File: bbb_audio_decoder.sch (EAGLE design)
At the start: 185 parts, among them IC1 OPA2134, IC2 LM317, IC3 LM337, IC4 OPA2134, IC5 OPA2134, IC6 OPA2134, IC7 LM317, P1 PLR135/T9, Q2 BS170, U1 PCM1690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

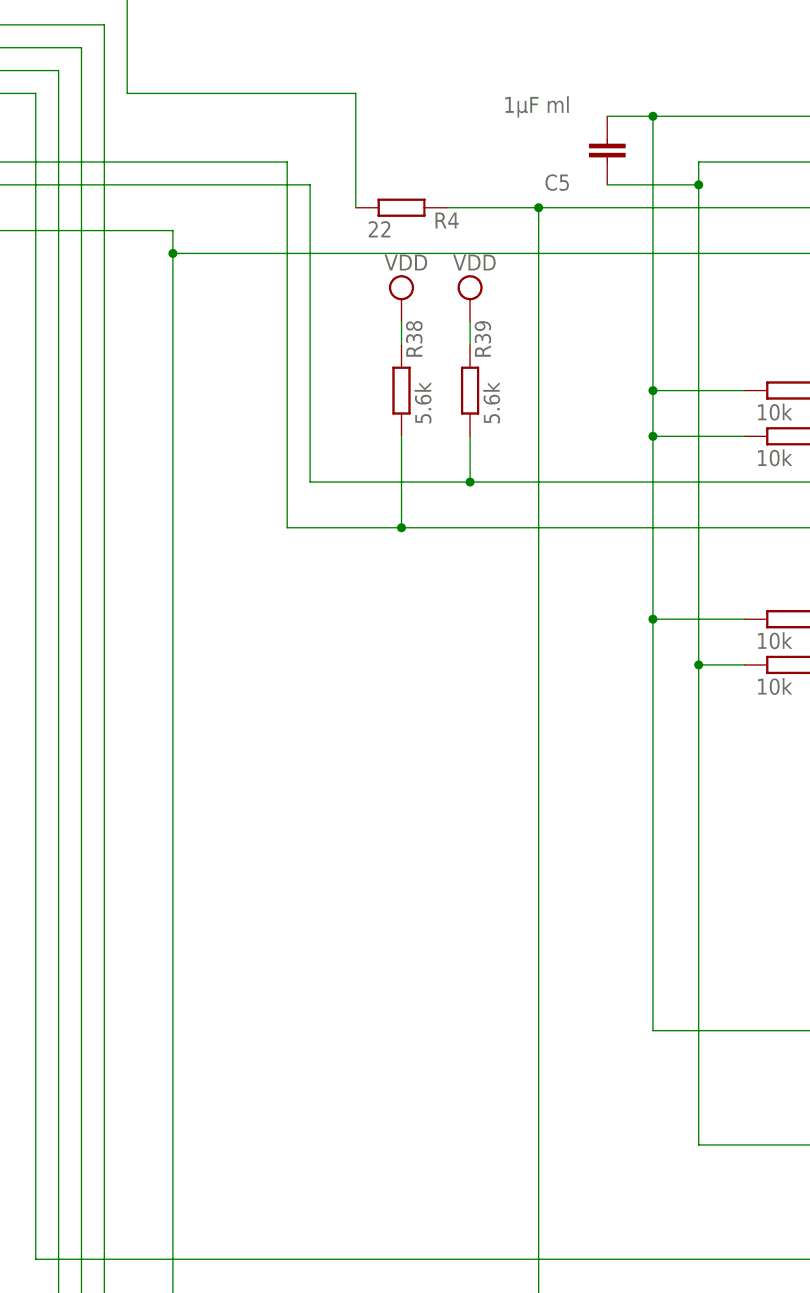
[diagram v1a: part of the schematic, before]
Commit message: Added molex 22-27-2041 connector for LCD
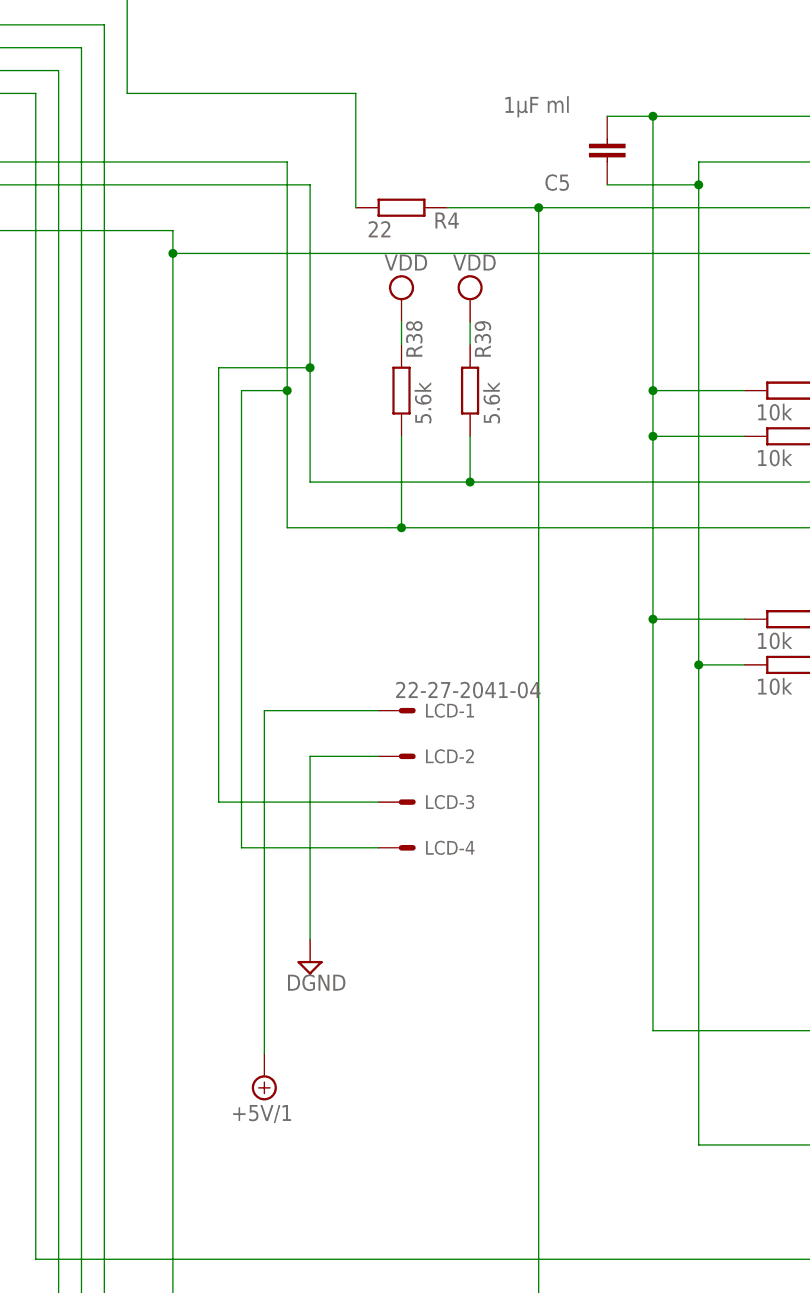
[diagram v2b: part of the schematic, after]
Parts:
- added LCD: 22-27-2041-04, con-molex:22-27-2041-04
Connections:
- net DGND: now also LCD-2.S
- net SCL: now also LCD-4.S
- net SDA: now also LCD-3.S
- net VDD_5V: now also LCD-1.S
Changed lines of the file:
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@@
 <grid distance="0.1" unitdist="inch" unit="inch" style="lines" multiple="1" display="no" altdistance="0.01" altunitdist="inch" altunit="inch"/>
 <layers>
-<layer number="1" name="Top" color="4" fill="1" visible="yes" active="no"/>
-<layer number="2" name="Route2" color="1" fill="3" visible="yes" active="no"/>
-<layer number="3" name="Route3" color="4" fill="3" visible="yes" active="no"/>
-<layer number="14" name="Route14" color="1" fill="6" visible="yes" active="no"/>
-<layer number="15" name="Route15" color="4" fill="6" visible="yes" active="no"/>
-<layer number="16" name="Bottom" color="1" fill="1" visible="yes" active="no"/>
-<layer number="17" name="Pads" color="2" fill="1" visible="yes" active="no"/>
-<layer number="18" name="Vias" color="2" fill="1" visible="yes" active="no"/>
-<layer number="19" name="Unrouted" color="6" fill="1" visible="yes" active="no"/>
-<layer number="20" name="Dimension" color="15" fill="1" visible="yes" active="no"/>
-<layer number="21" name="tPlace" color="7" fill="1" visible="yes" active="no"/>
-<layer number="22" name="bPlace" color="7" fill="1" visible="yes" active="no"/>
-<layer number="23" name="tOrigins" color="15" fill="1" visible="yes" active="no"/>
-<layer number="24" name="bOrigins" color="15" fill="1" visible="yes" active="no"/>
-<layer number="25" name="tNames" color="7" fill="1" visible="yes" active="no"/>
-<layer number="26" name="bNames" color="7" fill="1" visible="yes" active="no"/>
-<layer number="27" name="tValues" color="7" fill="1" visible="yes" active="no"/>
-<layer number="28" name="bValues" color="7" fill="1" visible="yes" active="no"/>
+<layer number="1" name="Top" color="4" fill="1" visible="no" active="no"/>
+<layer number="2" name="Route2" color="1" fill="3" visible="no" active="no"/>
+<layer number="3" name="Route3" color="4" fill="3" visible="no" active="no"/>
+<layer number="14" name="Route14" color="1" fill="6" visible="no" active="no"/>
+<layer number="15" name="Route15" color="4" fill="6" visible="no" active="no"/>
+<layer number="16" name="Bottom" color="1" fill="1" visible="no" active="no"/>
+<layer number="17" name="Pads" color="2" fill="1" visible="no" active="no"/>
+<layer number="18" name="Vias" color="2" fill="1" visible="no" active="no"/>
+<layer number="19" name="Unrouted" color="6" fill="1" visible="no" active="no"/>
+<layer number="20" name="Dimension" color="15" fill="1" visible="no" active="no"/>
+<layer number="21" name="tPlace" color="7" fill="1" visible="no" active="no"/>
+<layer number="22" name="bPlace" color="7" fill="1" visible="no" active="no"/>
+<layer number="23" name="tOrigins" color="15" fill="1" visible="no" active="no"/>
+<layer number="24" name="bOrigins" color="15" fill="1" visible="no" active="no"/>
+<layer number="25" name="tNames" color="7" fill="1" visible="no" active="no"/>
+<layer number="26" name="bNames" color="7" fill="1" visible="no" active="no"/>
+<layer number="27" name="tValues" color="7" fill="1" visible="no" active="no"/>
+<layer number="28" name="bValues" color="7" fill="1" visible="no" active="no"/>
 <layer number="29" name="tStop" color="7" fill="3" visible="no" active="no"/>
 <layer number="30" name="bStop" color="7" fill="6" visible="no" active="no"/>
@@
 <layer number="35" name="tGlue" color="7" fill="4" visible="no" active="no"/>
 <layer number="36" name="bGlue" color="7" fill="5" visible="no" active="no"/>
-<layer number="37" name="tTest" color="7" fill="1" visible="yes" active="no"/>
-<layer number="38" name="bTest" color="7" fill="1" visible="yes" active="no"/>
+<layer number="37" name="tTest" color="7" fill="1" visible="no" active="no"/>
+<layer number="38" name="bTest" color="7" fill="1" visible="no" active="no"/>
 <layer number="39" name="tKeepout" color="4" fill="11" visible="no" active="no"/>
 <layer number="40" name="bKeepout" color="1" fill="11" visible="no" active="no"/>
@@
 <layer number="44" name="Drills" color="7" fill="1" visible="no" active="no"/>
 <layer number="45" name="Holes" color="7" fill="1" visible="no" active="no"/>
-<layer number="46" name="Milling" color="3" fill="1" visible="yes" active="no"/>
-<layer number="47" name="Measures" color="7" fill="1" visible="yes" active="no"/>
-<layer number="48" name="Document" color="7" fill="1" visible="yes" active="no"/>
-<layer number="49" name="Reference" color="7" fill="1" visible="yes" active="no"/>
-<layer number="51" name="tDocu" color="7" fill="1" visible="yes" active="no"/>
-<layer number="52" name="bDocu" color="7" fill="1" visible="yes" active="no"/>
+<layer number="46" name="Milling" color="3" fill="1" visible="no" active="no"/>
+<layer number="47" name="Measures" color="7" fill="1" visible="no" active="no"/>
+<layer number="48" name="Document" color="7" fill="1" visible="no" active="no"/>
+<layer number="49" name="Reference" color="7" fill="1" visible="no" active="no"/>
+<layer number="51" name="tDocu" color="7" fill="1" visible="no" active="no"/>
+<layer number="52" name="bDocu" color="7" fill="1" visible="no" active="no"/>
 <layer number="90" name="Modules" color="5" fill="1" visible="yes" active="yes"/>
 <layer number="91" name="Nets" color="2" fill="1" visible="yes" active="yes"/>
@@
 <part name="SUPPLY53" library="supply2" deviceset="AGND" device=""/>
 <part name="SUPPLY56" library="supply2" deviceset="DGND" device=""/>
+<part name="SUPPLY58" library="supply2" deviceset="DGND" device=""/>
+<part name="LCD" library="con-molex" deviceset="22-?-04" device="27-2041"/>
+<part name="SUPPLY57" library="supply2" deviceset="+5V/1" device=""/>
 </parts>
 <sheets>
@@
 <instance part="SUPPLY53" gate="G$1" x="-5.08" y="246.38"/>
 <instance part="SUPPLY56" gate="G$1" x="114.3" y="251.46"/>
+<instance part="SUPPLY58" gate="G$1" x="12.7" y="-30.48"/>
+<instance part="LCD" gate="-1" x="22.86" y="-2.54"/>
+<instance part="LCD" gate="-2" x="22.86" y="-7.62"/>
+<instance part="LCD" gate="-3" x="22.86" y="-12.7"/>
+<instance part="LCD" gate="-4" x="22.86" y="-17.78"/>
+<instance part="SUPPLY57" gate="G$1" x="7.62" y="-43.18" rot="R180"/>
 </instances>
 <busses>
@@
 <wire x1="106.68" y1="254" x2="114.3" y2="254" width="0.1524" layer="91"/>
 <junction x="106.68" y="254"/>
+</segment>
+<segment>
+<pinref part="SUPPLY58" gate="G$1" pin="DGND"/>
+<wire x1="20.32" y1="-7.62" x2="12.7" y2="-7.62" width="0.1524" layer="91"/>
+<wire x1="12.7" y1="-7.62" x2="12.7" y2="-27.94" width="0.1524" layer="91"/>
+<pinref part="LCD" gate="-2" pin="S"/>
 </segment>
 </net>
@@
 <wire x1="76.2" y1="17.78" x2="22.86" y2="17.78" width="0.1524" layer="91"/>
 <wire x1="22.86" y1="17.78" x2="10.16" y2="17.78" width="0.1524" layer="91"/>
-<wire x1="10.16" y1="17.78" x2="10.16" y2="58.42" width="0.1524" layer="91"/>
+<wire x1="10.16" y1="17.78" x2="10.16" y2="33.02" width="0.1524" layer="91"/>
+<wire x1="10.16" y1="33.02" x2="10.16" y2="58.42" width="0.1524" layer="91"/>
 <wire x1="10.16" y1="58.42" x2="-35.56" y2="58.42" width="0.1524" layer="91"/>
 <pinref part="R38" gate="G$1" pin="1"/>
@@
 <junction x="22.86" y="17.78"/>
 <pinref part="U$1" gate="G$1" pin="I2C_SCL"/>
+<wire x1="10.16" y1="33.02" x2="5.08" y2="33.02" width="0.1524" layer="91"/>
+<wire x1="5.08" y1="33.02" x2="5.08" y2="-17.78" width="0.1524" layer="91"/>
+<junction x="10.16" y="33.02"/>
+<wire x1="5.08" y1="-17.78" x2="20.32" y2="-17.78" width="0.1524" layer="91"/>
+<pinref part="LCD" gate="-4" pin="S"/>
 </segment>
 </net>
@@
 <wire x1="12.7" y1="22.86" x2="30.48" y2="22.86" width="0.1524" layer="91"/>
 <wire x1="30.48" y1="22.86" x2="76.2" y2="22.86" width="0.1524" layer="91"/>
-<wire x1="12.7" y1="22.86" x2="12.7" y2="55.88" width="0.1524" layer="91"/>
+<wire x1="12.7" y1="22.86" x2="12.7" y2="35.56" width="0.1524" layer="91"/>
+<wire x1="12.7" y1="35.56" x2="12.7" y2="55.88" width="0.1524" layer="91"/>
 <wire x1="12.7" y1="55.88" x2="-35.56" y2="55.88" width="0.1524" layer="91"/>
 <pinref part="R39" gate="G$1" pin="1"/>
@@
 <junction x="30.48" y="22.86"/>
 <pinref part="U$1" gate="G$1" pin="I2C_SDA"/>
+<junction x="12.7" y="35.56"/>
+<wire x1="12.7" y1="35.56" x2="2.54" y2="35.56" width="0.1524" layer="91"/>
+<wire x1="2.54" y1="35.56" x2="2.54" y2="-12.7" width="0.1524" layer="91"/>
+<wire x1="2.54" y1="-12.7" x2="20.32" y2="-12.7" width="0.1524" layer="91"/>
+<pinref part="LCD" gate="-3" pin="S"/>
 </segment>
 </net>
@@
 <junction x="106.68" y="281.94"/>
 </segment>
-</net>
+<segment>
+<pinref part="LCD" gate="-1" pin="S"/>
+<pinref part="SUPPLY57" gate="G$1" pin="+5V/1"/>
+<wire x1="20.32" y1="-2.54" x2="7.62" y2="-2.54" width="0.1524" layer="91"/>
+<wire x1="7.62" y1="-2.54" x2="7.62" y2="-40.64" width="0.1524" layer="91"/>
+</segment>
+</net>

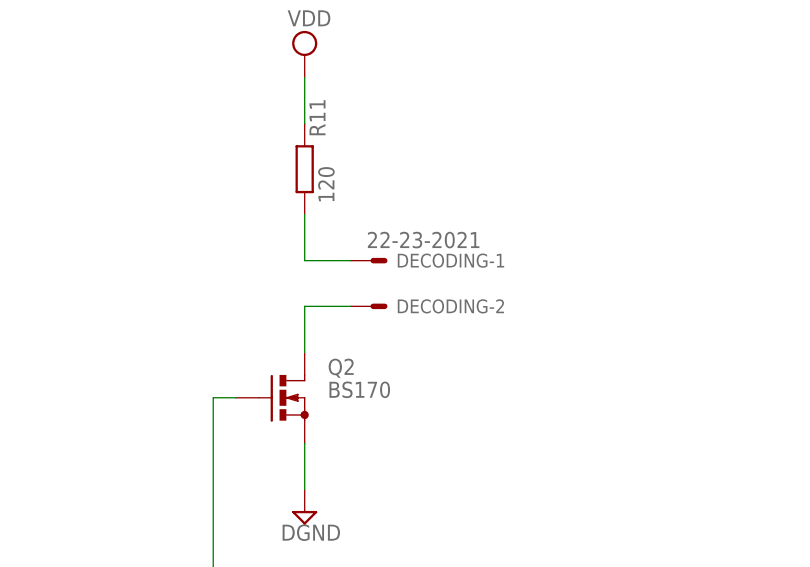
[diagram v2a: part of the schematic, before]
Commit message: Replaced LED with 1206 SMD one
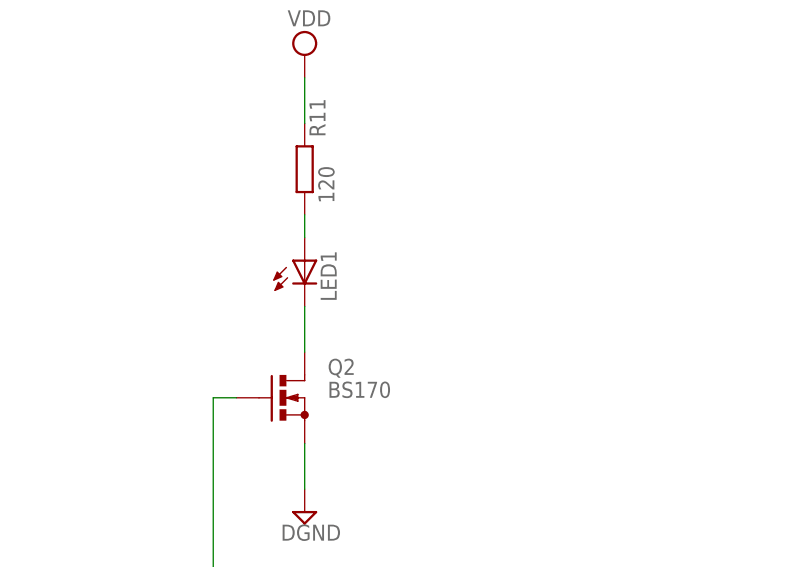
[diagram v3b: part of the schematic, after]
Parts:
- removed DECODING: 22-23-2021, con-molex:22-23-2021
- added LED1: (no value), led:LEDSMT1206
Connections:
- removed net N$91: DECODING-2.S, Q2.D
- removed net N$92: DECODING-1.S, R11.1
- new net N$28: LED1.C, Q2.D
- new net N$4: LED1.A, R11.1
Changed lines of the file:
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@@
 <part name="R11" library="rcl" deviceset="R-EU_" device="0204/2V" value="120"/>
 <part name="SUPPLY55" library="supply2" deviceset="VDD" device=""/>
-<part name="DECODING" library="con-molex" deviceset="22-23-2021" device=""/>
 <part name="OUT1" library="con-molex" deviceset="22-23-2021" device=""/>
 <part name="OUT2" library="con-molex" deviceset="22-23-2021" device=""/>
@@
 <part name="LCD" library="con-molex" deviceset="22-?-04" device="27-2041"/>
 <part name="SUPPLY57" library="supply2" deviceset="+5V/1" device=""/>
+<part name="LED1" library="led" deviceset="LED" device="SMT1206"/>
 </parts>
 <sheets>
@@
 </instance>
 <instance part="SUPPLY55" gate="G$1" x="5.08" y="154.94"/>
-<instance part="DECODING" gate="-1" x="12.7" y="132.08"/>
-<instance part="DECODING" gate="-2" x="12.7" y="127"/>
 <instance part="OUT1" gate="-1" x="335.28" y="167.64"/>
 <instance part="OUT1" gate="-2" x="335.28" y="172.72"/>
@@
 <instance part="LCD" gate="-4" x="22.86" y="-17.78"/>
 <instance part="SUPPLY57" gate="G$1" x="7.62" y="-43.18" rot="R180"/>
+<instance part="LED1" gate="G$1" x="5.08" y="132.08"/>
 </instances>
 <busses>
@@
 </segment>
 </net>
-<net name="N$91" class="0">
-<segment>
-<pinref part="Q2" gate="1" pin="D"/>
-<wire x1="5.08" y1="121.92" x2="5.08" y2="127" width="0.1524" layer="91"/>
-<pinref part="DECODING" gate="-2" pin="S"/>
-<wire x1="10.16" y1="127" x2="5.08" y2="127" width="0.1524" layer="91"/>
-</segment>
-</net>
-<net name="N$92" class="0">
-<segment>
-<pinref part="R11" gate="G$1" pin="1"/>
-<pinref part="DECODING" gate="-1" pin="S"/>
-<wire x1="10.16" y1="132.08" x2="5.08" y2="132.08" width="0.1524" layer="91"/>
-<wire x1="5.08" y1="132.08" x2="5.08" y2="137.16" width="0.1524" layer="91"/>
-</segment>
-</net>
 <net name="N$94" class="0">
 <segment>
@@
 </segment>
 </net>
+<net name="N$4" class="0">
+<segment>
+<pinref part="R11" gate="G$1" pin="1"/>
+<pinref part="LED1" gate="G$1" pin="A"/>
+<wire x1="5.08" y1="137.16" x2="5.08" y2="134.62" width="0.1524" layer="91"/>
+</segment>
+</net>
+<net name="N$28" class="0">
+<segment>
+<pinref part="LED1" gate="G$1" pin="C"/>
+<pinref part="Q2" gate="1" pin="D"/>
+<wire x1="5.08" y1="127" x2="5.08" y2="121.92" width="0.1524" layer="91"/>
+</segment>
+</net>

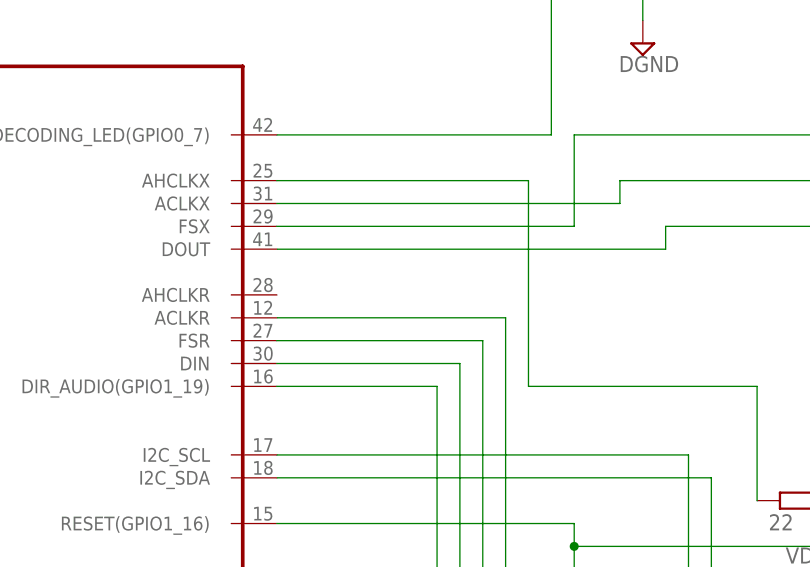
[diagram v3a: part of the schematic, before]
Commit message: Connect DIR9001 SCKO to AHCLKR as well.
This is a follow-up of commit c6b4b11, where I apparently only connected
the recovered clock from the DIR9001 to AHCLKX.
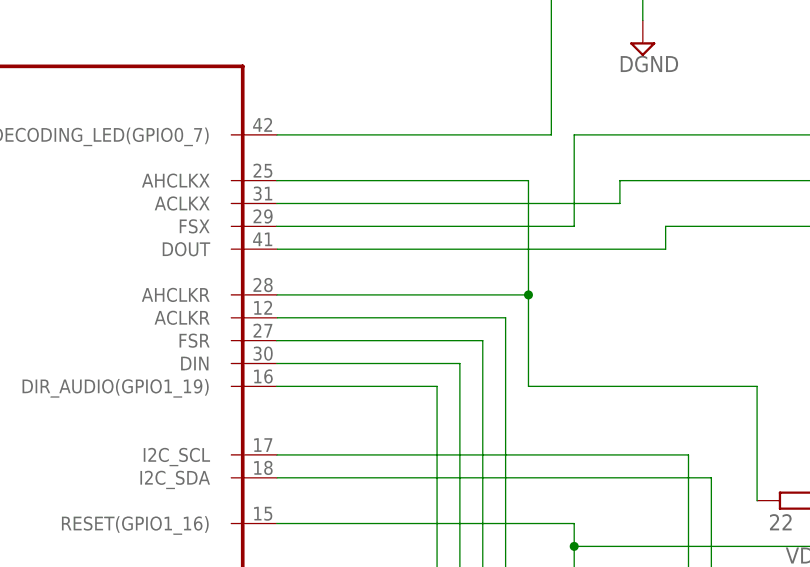
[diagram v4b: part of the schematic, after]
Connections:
- net MCLK: now also U$1.AHCLKR
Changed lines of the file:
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@@
 <wire x1="17.78" y1="53.34" x2="17.78" y2="66.04" width="0.1524" layer="91"/>
 <wire x1="17.78" y1="66.04" x2="-7.62" y2="66.04" width="0.1524" layer="91"/>
-<wire x1="-7.62" y1="66.04" x2="-7.62" y2="88.9" width="0.1524" layer="91"/>
+<wire x1="-7.62" y1="66.04" x2="-7.62" y2="76.2" width="0.1524" layer="91"/>
+<wire x1="-7.62" y1="76.2" x2="-7.62" y2="88.9" width="0.1524" layer="91"/>
 <wire x1="-7.62" y1="88.9" x2="-35.56" y2="88.9" width="0.1524" layer="91"/>
 <pinref part="U$1" gate="G$1" pin="AHCLKX"/>
+<pinref part="U$1" gate="G$1" pin="AHCLKR"/>
+<wire x1="-35.56" y1="76.2" x2="-7.62" y2="76.2" width="0.1524" layer="91"/>
+<junction x="-7.62" y="76.2"/>
 </segment>
 </net>
